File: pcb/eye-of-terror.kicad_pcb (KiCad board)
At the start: 4 copper layers, 200 x 200 mm, 225 parts, among them J1 Conn_01x02_Socket, J2 G-Switch GT-USB-7055E, J3 Conn_01x04, J4 Conn_01x04, J5 Conn_01x03, J6 Conn_01x02_Socket, J7 Conn_01x02_Socket, J8 Conn_01x03, Q1 IPT020N10N3, Q10 ALS-PT19-315C/L177/TR8, Q11 ALS-PT19-315C/L177/TR8, Q12 ALS-PT19-315C/L177/TR8, Q13 ALS-PT19-315C/L177/TR8, Q14 ALS-PT19-315C/L177/TR8, Q15 ALS-PT19-315C/L177/TR8, Q16 ALS-PT19-315C/L177/TR8, Q17 ALS-PT19-315C/L177/TR8, Q2 IPT020N10N3, Q3 IPT020N10N3, Q4 IPT020N10N3, Q5 IPT020N10N3, Q6 IPT020N10N3, Q7 ALS-PT19-315C/L177/TR8, Q8 ALS-PT19-315C/L177/TR8, Q9 ALS-PT19-315C/L177/TR8, SW1 SW_Push, SW2 SW_Push, U1 RP2350B, U2 TD1660, U3 AP63205WU-7, U4 LSM6DS3, U5 W25Q32JVSS, U7 DRV8353HRTAR, Y1 ABM8-272-T3

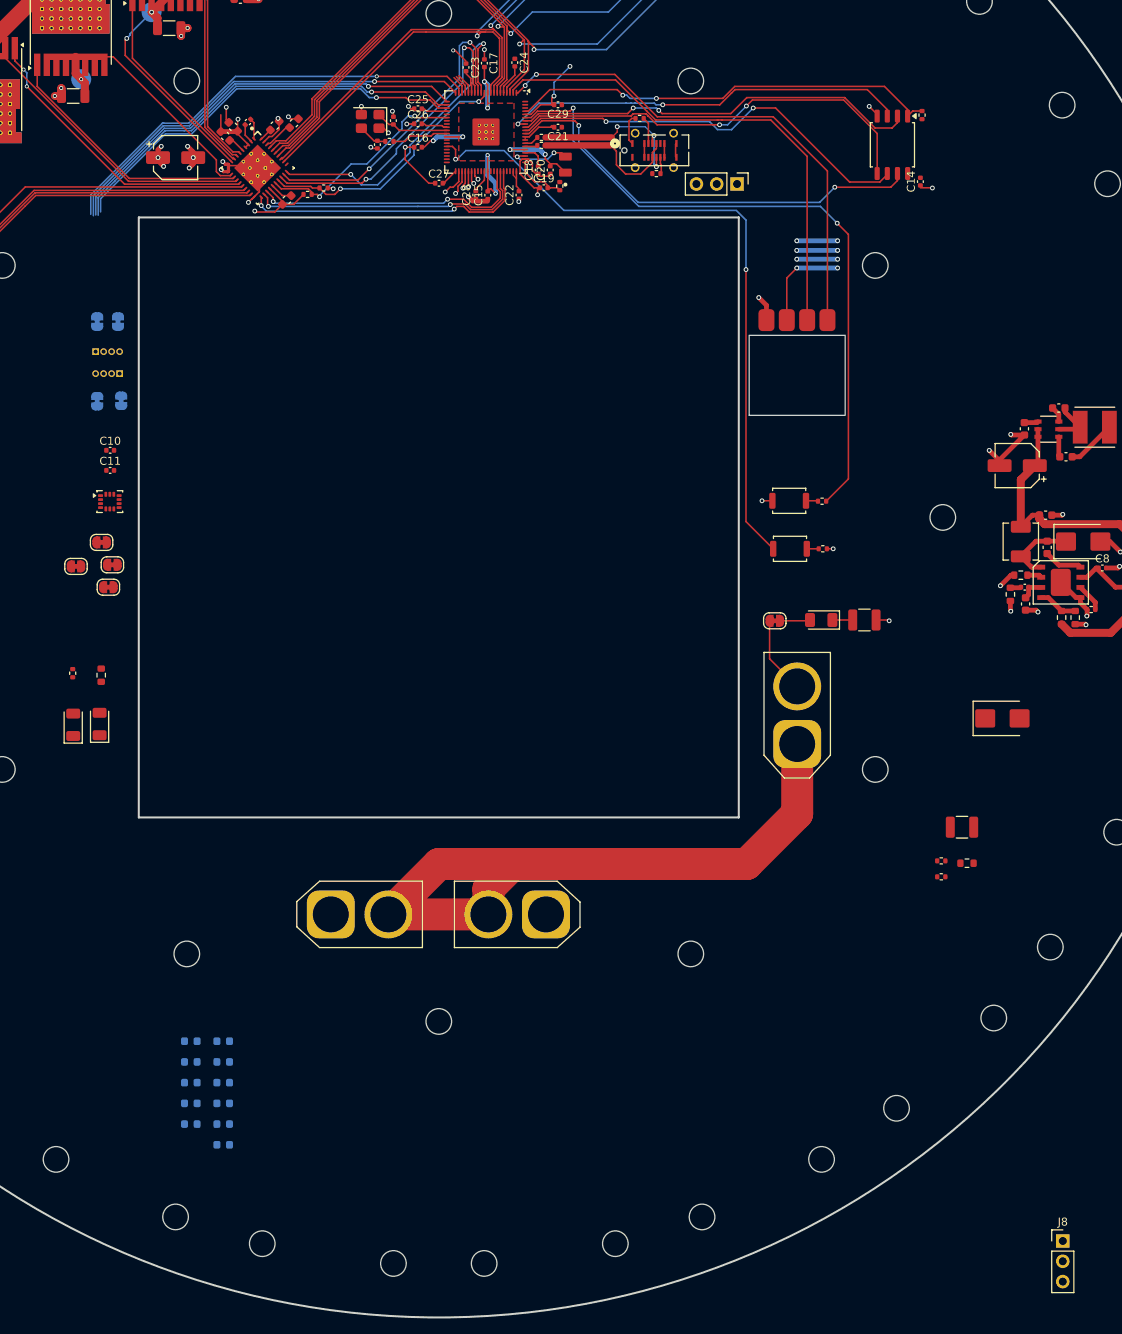
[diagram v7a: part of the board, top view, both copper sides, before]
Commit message: routed IR TOF sensors and IMU
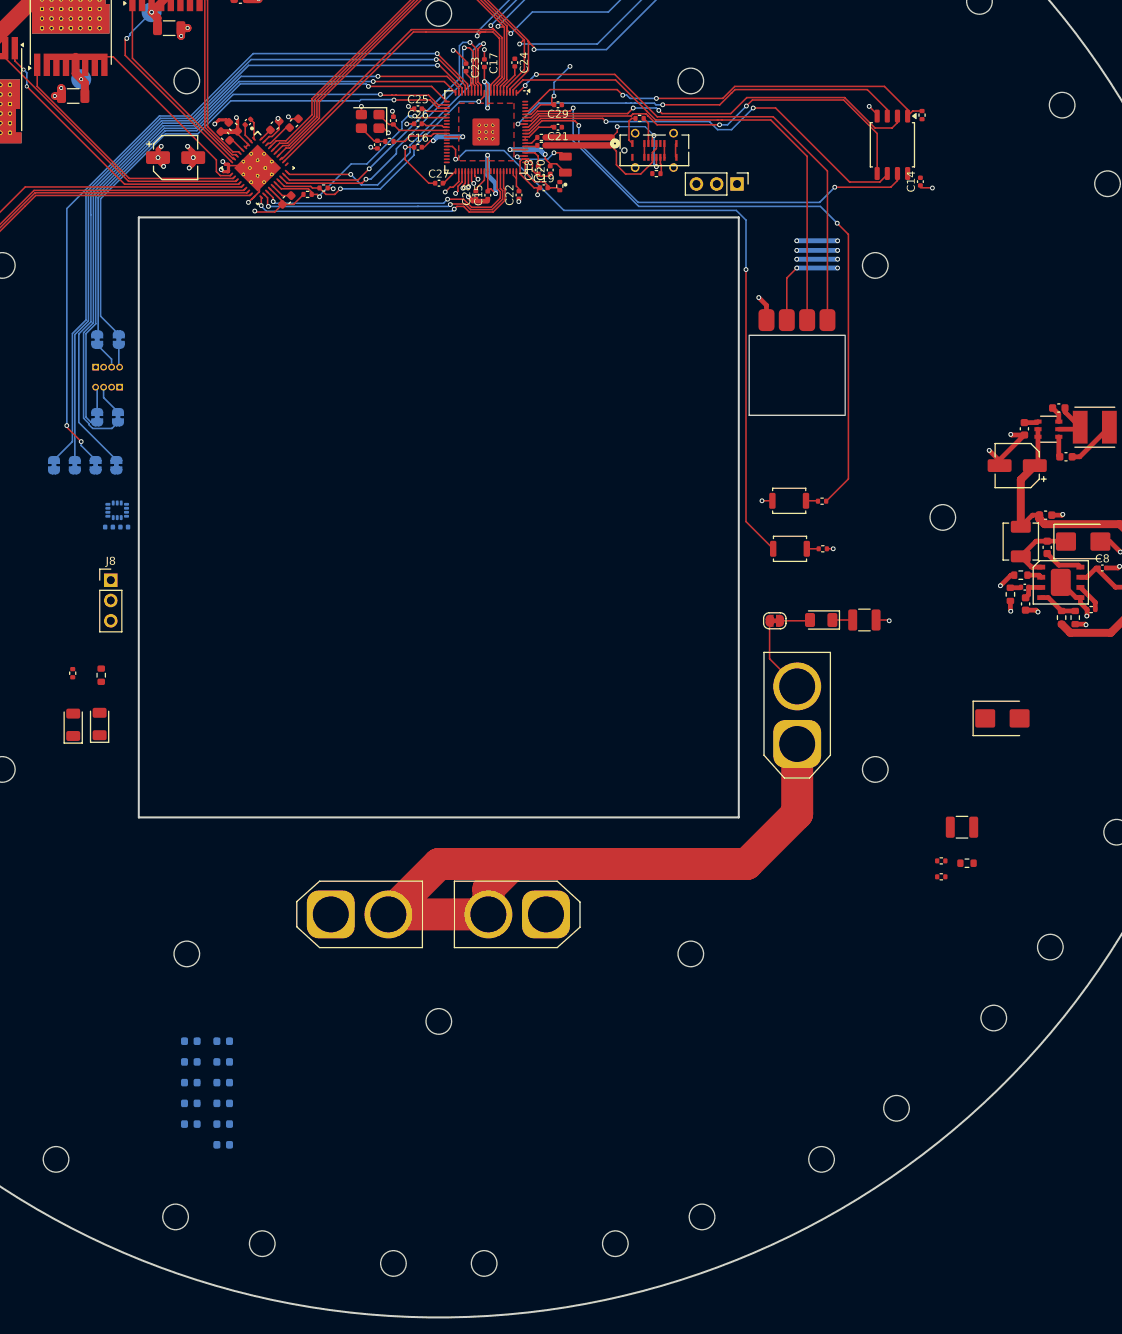
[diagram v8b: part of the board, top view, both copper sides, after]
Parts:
- C10, C11, JP4, JP5, JP6, JP7, U4: moved to B.Cu
- moved J8 144.9 mm to (267.7, 206.9)
- moved JP4 15.3 mm to (265.8, 192.6), turned to -90 degrees
- moved JP7 12.9 mm to (260.6, 192.6), turned to -90 degrees
- moved JP5 12.5 mm to (268.4, 192.6), turned to -90 degrees
- moved JP1 12.2 mm to (268.6, 186.6), turned to 90 degrees
- moved JP9 12.2 mm to (266.0, 186.6), turned to 90 degrees
- moved JP6 10.2 mm to (263.2, 192.6), turned to -90 degrees
- moved C10 9.60 mm to (267.5, 200.3), turned to 180 degrees
- moved JP2 7.70 mm to (266.0, 176.8), turned to -90 degrees
- moved JP3 7.66 mm to (268.7, 176.8), turned to -90 degrees
- moved C11 7.30 mm to (269.4, 200.3)
- moved J3 5.37 mm to (268.8, 182.8), turned to 90 degrees
- moved J4 3.10 mm to (265.8, 180.3), turned to -90 degrees
- moved U4 1.43 mm to (268.5, 198.2), turned to 180 degrees
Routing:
- net PGND: track 54.5 -> 157.9 mm
- net /IMU_CIPO: track 2.65 -> 93.8 mm, vias 0 -> 3
- net /IMU_CS: track 2.48 -> 91.6 mm, vias 0 -> 1
- net /IMU_SCK: track 2.31 -> 89.1 mm, vias 0 -> 1
- net /IMU_COPI: track 55.8 -> 89.1 mm
- net /SDA_TOP_IR_TOF: track 54.3 -> 85.3 mm
- net /SCL_TOP_IR_TOF: track 52.9 -> 80.4 mm
- net /SCL_BOT_IR_TOF: track 51.6 -> 66.8 mm
- net /SDA_BOT_IR_TOF: track 52.5 -> 66.6 mm
- net Net-(J3-Pin_3): track 0.00 -> 3.85 mm
- net Net-(J4-Pin_3): track 0.00 -> 3.55 mm
- net Net-(J3-Pin_4): track 0.00 -> 3.18 mm
- net Net-(J4-Pin_4): track 0.00 -> 2.84 mm
- net +BATT: track 48.1 -> 46.2 mm
